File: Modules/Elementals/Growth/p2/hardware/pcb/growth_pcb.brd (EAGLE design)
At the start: 17.8 x 101.9 mm, 20 parts, among them J1 EURO_POWER, J2 WQP-PJ398SM6, J3 WQP-PJ398SM6, J4 WQP-PJ398SM6, J5 WQP-PJ398SM6, U1 TL072P

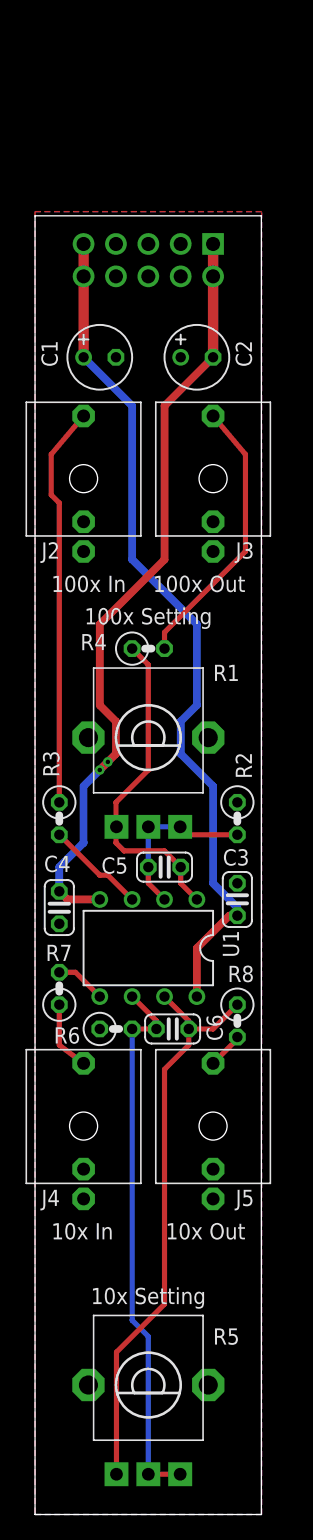
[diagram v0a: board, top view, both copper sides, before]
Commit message: Replaced board holes/outlines with standard library component
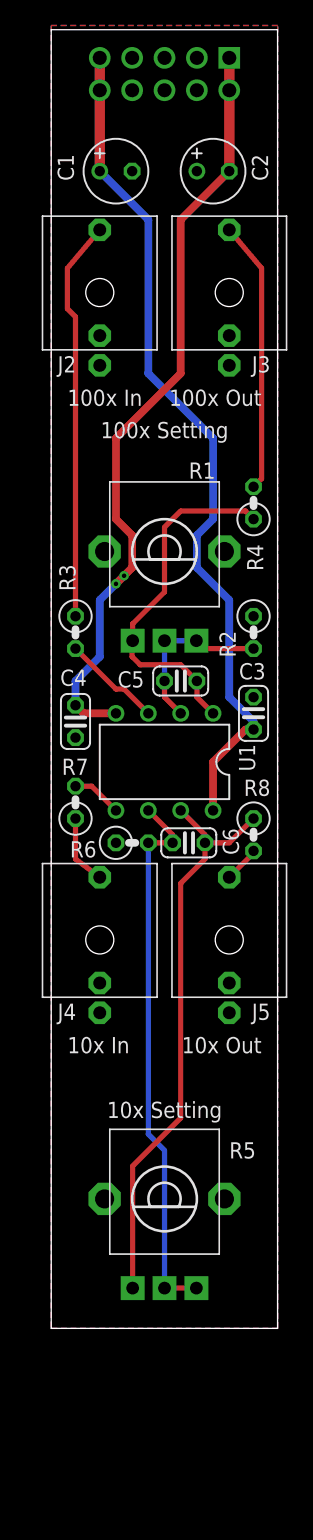
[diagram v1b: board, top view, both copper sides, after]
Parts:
- added U$1: (no value), SonicAthame:PANEL_REF_4U
- added U$2: (no value), SonicAthame:LOGO-65MIL-BSILK
- moved C3 14.7 mm to (17.1, 62.9)
- moved C5 14.7 mm to (11.4, 65.4)
- moved J1 14.7 mm to (10.2, 113.0)
- moved J2 14.7 mm to (5.08, 95.9)
- moved J3 14.7 mm to (15.2, 95.9)
- moved R2 14.7 mm to (17.1, 69.2)
- moved R3 14.7 mm to (3.17, 69.2)
- moved R7 14.7 mm to (3.17, 55.9)
- moved R8 14.7 mm to (17.1, 53.3)
- moved J4 14.7 mm to (5.08, 45.1)
- moved J5 14.7 mm to (15.2, 45.1)
- moved R5 14.7 mm to (10.2, 24.8)
- moved C4 14.7 mm to (3.17, 62.2)
- moved C6 14.7 mm to (12.1, 52.7)
- moved R1 14.7 mm to (10.2, 75.6)
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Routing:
- net N$2: track 25.8 -> 28.0 mm
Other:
- board text removed: "Sonic Athame™"
- board text removed: "The Point of Modular"

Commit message: Reposition
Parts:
- moved C1 3.81 mm to (6.35, 101.6)
- moved C2 3.81 mm to (14.0, 101.6)
- moved C3 3.81 mm to (17.1, 59.1)
- moved C5 3.81 mm to (11.4, 61.6)
- moved J1 3.81 mm to (10.2, 109.2)
- moved J2 3.81 mm to (5.08, 92.1)
- moved J3 3.81 mm to (15.2, 92.1)
- moved J4 3.81 mm to (5.08, 41.3)
- moved J5 3.81 mm to (15.2, 41.3)
- moved R1 3.81 mm to (10.2, 71.8)
- moved R2 3.81 mm to (17.1, 65.4)
- moved R3 3.81 mm to (3.17, 65.4)
- moved R4 3.81 mm to (17.1, 75.6)
- moved R5 3.81 mm to (10.2, 21.0)
- moved R7 3.81 mm to (3.17, 52.1)
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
